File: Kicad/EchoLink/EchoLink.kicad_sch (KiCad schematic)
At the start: 37 parts, among them U1 STM32L433CCT6

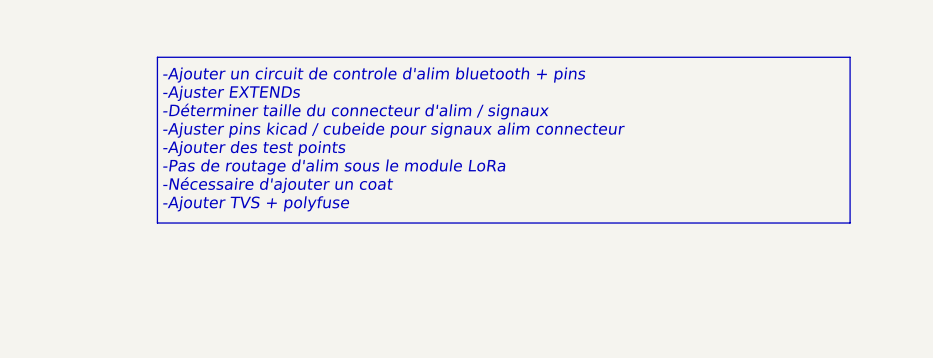
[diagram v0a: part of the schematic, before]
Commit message: wip: rename compoents
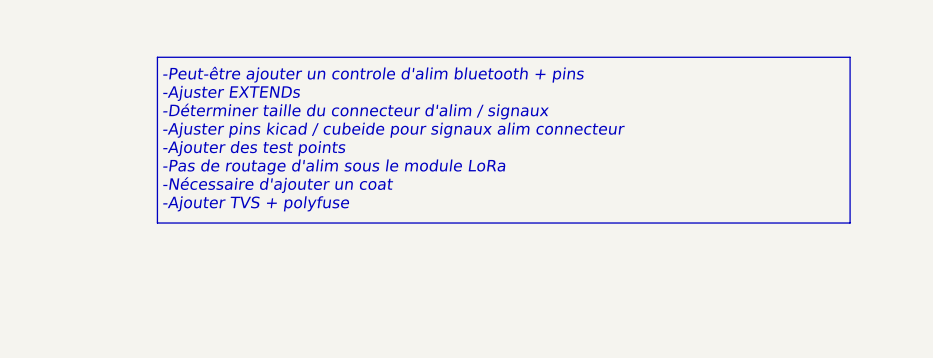
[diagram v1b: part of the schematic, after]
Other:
- note added: "-Peut-être ajouter un controle d'alim bluetooth + pins -Ajuster EXTENDs -Déterminer taille du connecteur d'alim / signaux -Ajuster pins kicad / cubeide pour signaux alim connecteur -Ajouter des test points -Pas de routage d'alim sous le module LoRa -Nécessaire d'ajouter un coat -Ajouter TVS + polyfuse"
- note removed: "-Ajouter un circuit de controle d'alim bluetooth + pins -Ajuster EXTENDs -Déterminer taille du connecteur d'alim / signaux -Ajuster pins kicad / cubeide pour signaux alim connecteur -Ajouter des test points -Pas de routage d'alim sous le module LoRa -Nécessaire d'ajouter un coat -Ajouter TVS + polyfuse"
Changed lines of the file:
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@@
 		)
 	)
-	(text "-Ajouter un circuit de controle d'alim bluetooth + pins\n-Ajuster EXTENDs\n-Déterminer taille du connecteur d'alim / signaux\n-Ajuster pins kicad / cubeide pour signaux alim connecteur\n-Ajouter des test points\n-Pas de routage d'alim sous le module LoRa\n-Nécessaire d'ajouter un coat\n-Ajouter TVS + polyfuse"
+	(text "-Peut-être ajouter un controle d'alim bluetooth + pins\n-Ajuster EXTENDs\n-Déterminer taille du connecteur d'alim / signaux\n-Ajuster pins kicad / cubeide pour signaux alim connecteur\n-Ajouter des test points\n-Pas de routage d'alim sous le module LoRa\n-Nécessaire d'ajouter un coat\n-Ajouter TVS + polyfuse"
 		(exclude_from_sim no)
 		(at 100.33 26.416 0)

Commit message: wip: connector and bms IOs
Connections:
- net EXTEND_IO1: no longer U1.30 (PA9)
- net EXTEND_IO2: no longer U1.31 (PA10)
- net EXTEND_IO3: no longer U1.32 (PA11)
- net EXTEND_IO4: no longer U1.33 (PA12)
- net POWER_IO1: no longer names the net of U1.5 (PH0-OSC_IN)
- net POWER_IO2: no longer names the net of U1.6 (PH1-OSC_OUT)
- net POWER_IO3: no longer names the net of U1.3 (PC14-OSC32_IN)
- net POWER_IO4: no longer names the net of U1.4 (PC15-OSC32_OUT)
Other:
- note added: "-Peut-être ajouter un controle d'alim bluetooth + pins -Ajuster EXTENDs -Connecteur entrant: 4x IOs relais (1x horn, 2x start engine, 1x start engine feedback) 1x UART/RS232/485/CAN -Pas de routage d'alim sous le module LoRa -Nécessaire d'ajouter un coat -Ajouter TVS + polyfuse -Possibilité de remplacer 3 entrées WKUP par 1 avec un OR 3-gates"
- note removed: "-Peut-être ajouter un controle d'alim bluetooth + pins -Ajuster EXTENDs -Déterminer taille du connecteur d'alim / signaux -Ajuster pins kicad / cubeide pour signaux alim connecteur -Ajouter des test points -Pas de routage d'alim sous le module LoRa -Nécessaire d'ajouter un coat -Ajouter TVS + polyfuse"

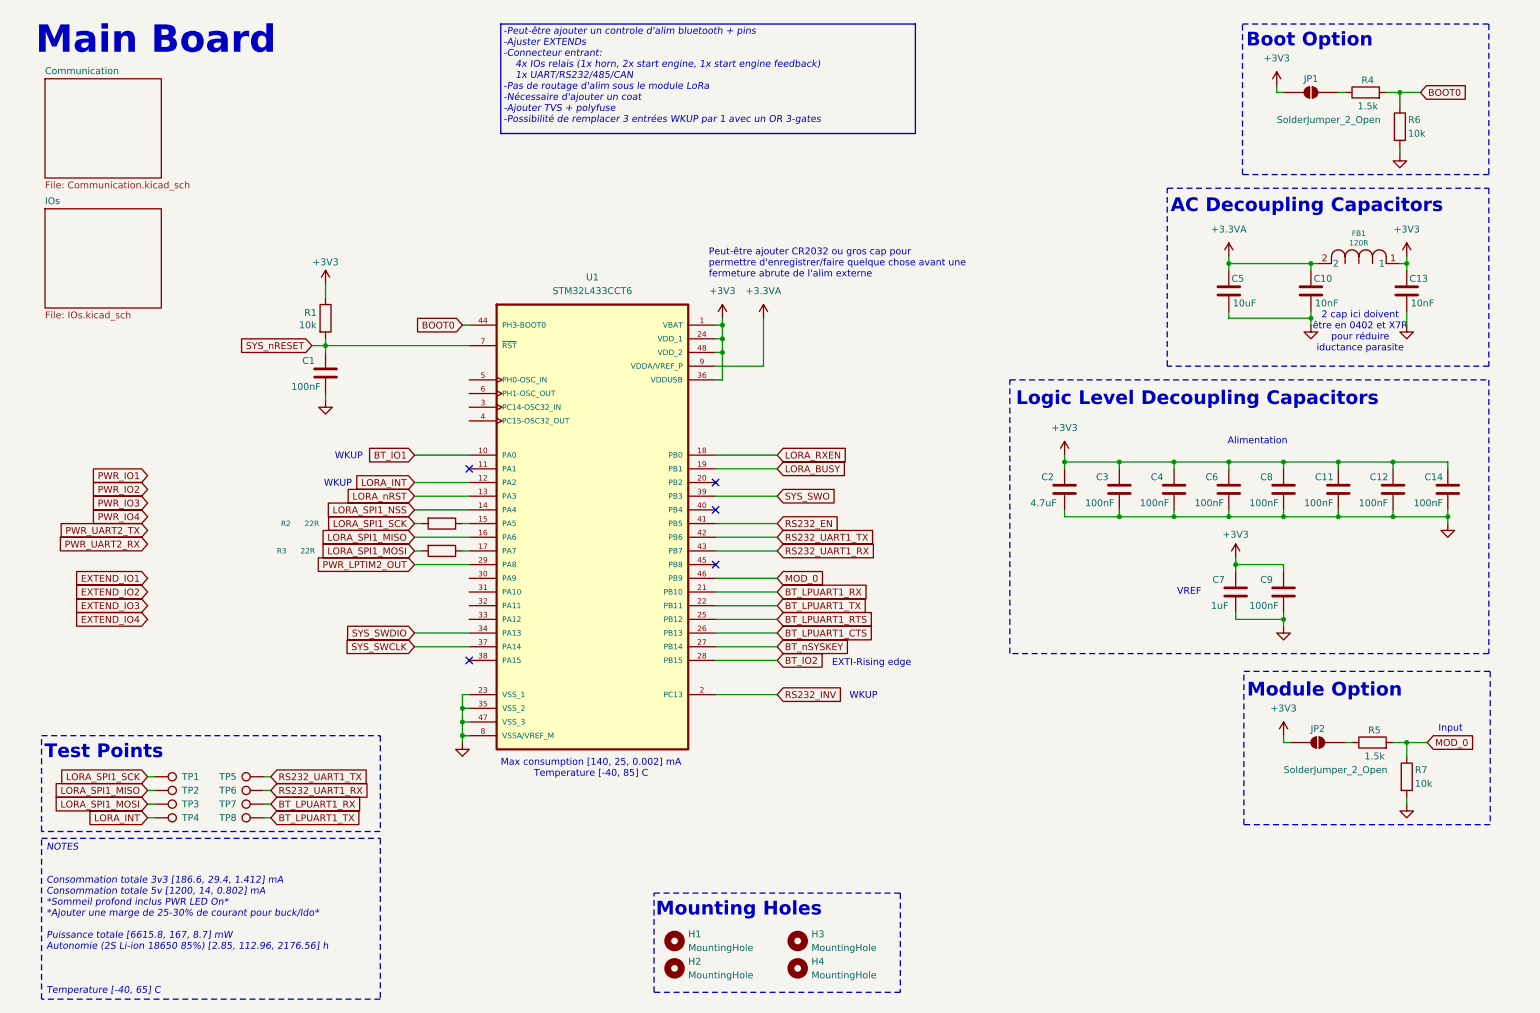
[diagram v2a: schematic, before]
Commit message: fix: rework all schematics to fit with new design and update stm32cubemx project
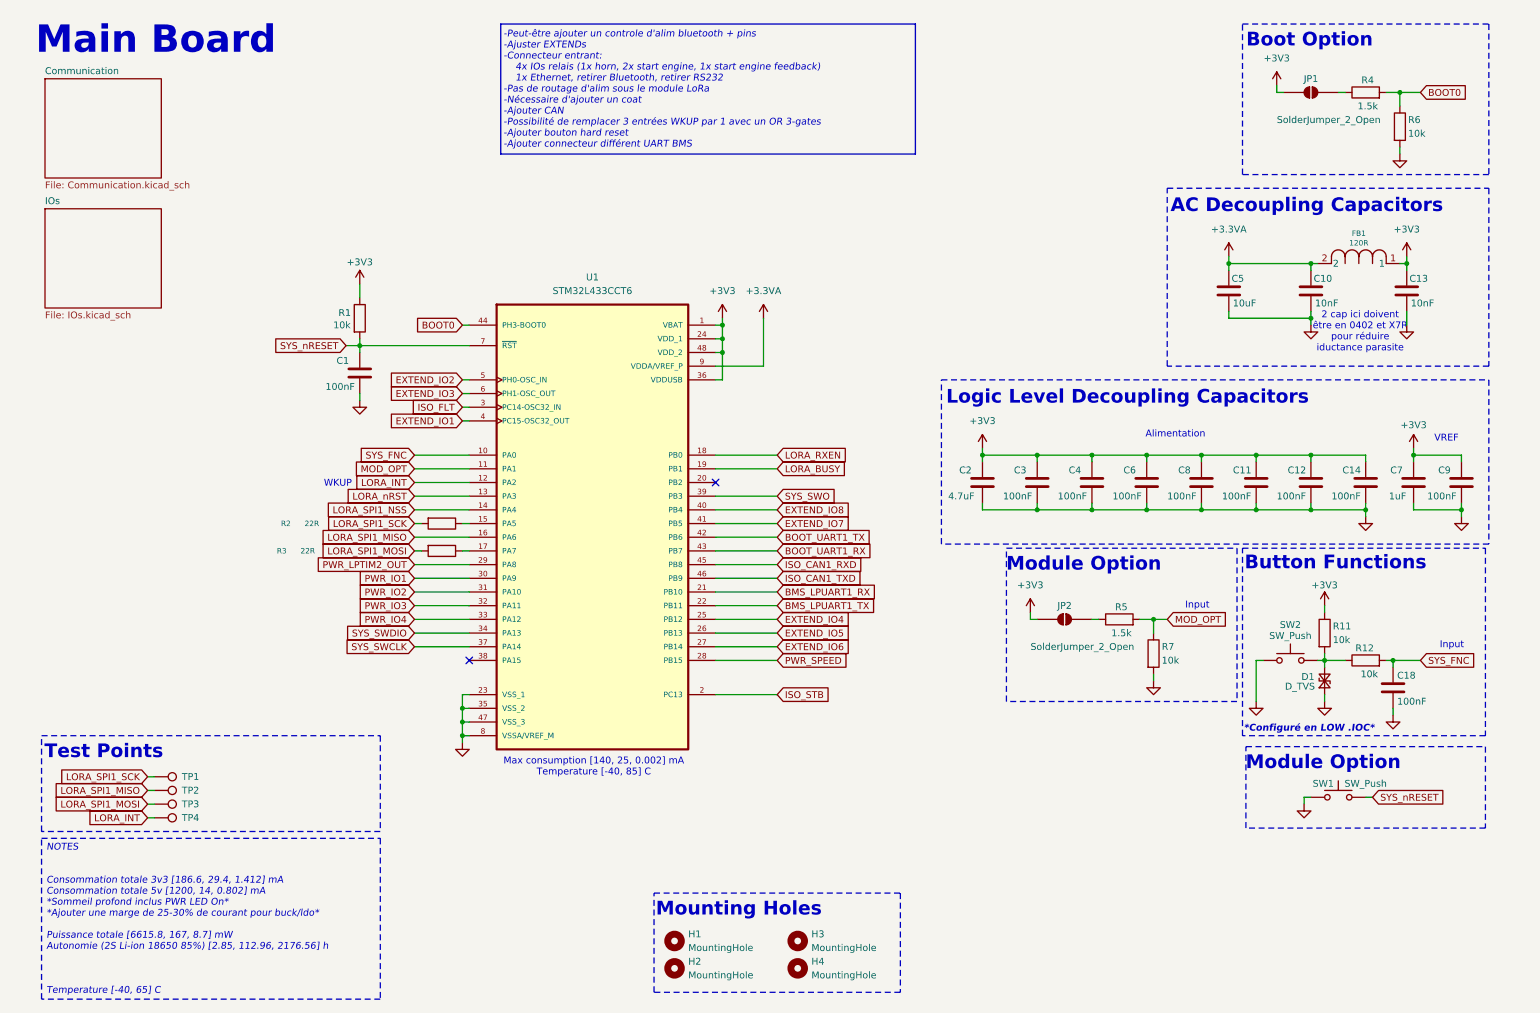
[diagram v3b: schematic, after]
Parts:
- removed TP5, TP6, TP7, TP8: TestPoint, TestPoint:TestPoint_Pad_D1.0mm, symbol Connector:TestPoint
- added C18: 100nF, Capacitor_SMD:C_0603_1608Metric, symbol Device:C
- added D1: D_TVS, symbol Device:D_TVS_Small
- added R11, R12: 10k, Resistor_SMD:R_0603_1608Metric, symbol Device:R
- added SW1, SW2: SW_Push, Package_SO:SOIC-8_3.9x4.9mm_P1.27mm, symbol Switch:SW_Push
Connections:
- net BT_LPUART1_RTS is gone; now on net EXTEND_IO4: U1.25 (PB12)
- net +3V3: now also R11.1
- net EXTEND_IO1: now also U1.4 (PC15-OSC32_OUT)
- net EXTEND_IO2: now also U1.5 (PH0-OSC_IN)
- net EXTEND_IO3: now also U1.6 (PH1-OSC_OUT)
- net GND: now also C18.2, D1.1 (A1), SW1.1, SW2.1
- net PWR_IO1: now also U1.30 (PA9)
- net PWR_IO2: now also U1.31 (PA10)
- net PWR_IO3: now also U1.32 (PA11)
- net PWR_IO4: now also U1.33 (PA12)
- net SYS_nRESET: now also SW1.2
- net MOD_OPT: now reaches U1.11 (PA1)
- net MOD_OPT: now also R5.2, R7.1
- net ISO_FLT: now reaches U1.3 (PC14-OSC32_IN)
- net EXTEND_IO8: now reaches U1.40 (PB4)
- net ISO_CAN1_RXD: now reaches U1.45 (PB8)
- net BT_IO1 renamed SYS_FNC
- net SYS_FNC: now also C18.1, R12.2
- net BT_IO2 renamed PWR_SPEED
- net BT_LPUART1_CTS renamed EXTEND_IO5
- net BT_LPUART1_RX renamed BMS_LPUART1_RX
- net BT_LPUART1_TX renamed BMS_LPUART1_TX
- net BT_nSYSKEY renamed EXTEND_IO6
- removed net MOD_0: R5.2, R7.1, U1.46 (PB9)
- net RS232_EN renamed EXTEND_IO7
- net RS232_INV renamed ISO_STB
- net RS232_UART1_RX renamed BOOT_UART1_RX
- net RS232_UART1_TX renamed BOOT_UART1_TX
- new net: D1.2 (A2), R11.2, R12.1, SW2.2
- new net ISO_CAN1_TXD: U1.46 (PB9)
- no-connect marks 5 -> 2
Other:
- note added: "*Configuré en LOW .IOC*"
- note added: "-Peut-être ajouter un controle d'alim bluetooth + pins -Ajuster EXTENDs -Connecteur entrant: 4x IOs relais (1x horn, 2x start engine, 1x start engine feedback) 1x Ethernet, retirer Bluetooth, retirer RS232 -Pas de routage d'alim sous le module LoRa -Nécessaire d'ajouter un coat -Ajouter CAN -Possibilité de remplacer 3 entrées WKUP par 1 avec un OR 3-gates -Ajouter bouton hard reset -Ajouter conne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"
- note added: "Button Functions"
- note removed: "-Peut-être ajouter un controle d'alim bluetooth + pins -Ajuster EXTENDs -Connecteur entrant: 4x IOs relais (1x horn, 2x start engine, 1x start engine feedback) 1x UART/RS232/485/CAN -Pas de routage d'alim sous le module LoRa -Nécessaire d'ajouter un coat -Ajouter TVS + polyfuse -Possibilité de remplacer 3 entrées WKUP par 1 avec un OR 3-gates"
- note removed: "EXTI-Rising edge"
- note removed: "Peut-être ajouter CR2032 ou gros cap pour permettre d'enregistrer/faire quelque chose avant une fermeture abrute de l'alim externe"
- moved on the sheet: C1, C11, C12, C14, C2, C3, C4, C6, C7, C8, C9, JP2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

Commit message: wip: add missing footprints
- connectors missing
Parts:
- added TP10, TP11, TP5, TP6, TP7, TP8, TP9: TestPoint, TestPoint:TestPoint_Pad_D1.0mm, symbol Connector:TestPoint
- D1, FB1: footprint (none) -> Resistor_SMD:R_0805_2012Metric
- SW1: renamed from SW2; footprint Package_SO:SOIC-8_3.9x4.9mm_P1.27mm -> EchoLink_Lib:SON4_PTS526 SM15 SMTR2 LFS_CNK
- SW2: renamed from SW1; footprint Package_SO:SOIC-8_3.9x4.9mm_P1.27mm -> EchoLink_Lib:SON4_PTS526 SM15 SMTR2 LFS_CNK
- U1: footprint STM32L433CCT6:QFP50P900X900X160-48N -> EchoLink_Lib:QFP50P900X900X160-48N
- renumbered C12 to C10, C14 to C11, C18 to C12, C7 to C14, C9 to C15, C6 to C5, C8 to C6, C5 to C7, C11 to C8, C10 to C9, JP2 to JP1, JP1 to JP2, R5 to R4, R7 to R5, R11 to R6, R4 to R7, R12 to R8, R6 to R9
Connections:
- net BMS_LPUART1_RX: now also TP9.1
- net BMS_LPUART1_TX: now also TP8.1
- net ISO_CAN1_RXD: now also TP5.1
- net ISO_CAN1_TXD: now also TP6.1
- net ISO_FLT renamed ISO_FNC
- net ISO_FNC: now also TP7.1
- new net EXTEND_UART1_RX: TP11.1
- new net EXTEND_UART1_TX: TP10.1
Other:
- note added: "-Pas de routage d'alim sous le module LoRa -Nécessaire d'ajouter un coat -Vérifier TVS"
- note removed: "-Peut-être ajouter un controle d'alim bluetooth + pins -Ajuster EXTENDs -Connecteur entrant: 4x IOs relais (1x horn, 2x start engine, 1x start engine feedback) 1x Ethernet, retirer Bluetooth, retirer RS232 -Pas de routage d'alim sous le module LoRa -Nécessaire d'ajouter un coat -Ajouter CAN -Possibilité de remplacer 3 entrées WKUP par 1 avec un OR 3-gates -Ajouter bouton hard reset -Ajouter conne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"
- note removed: "2 cap ici doivent être en 0402 et X7R pour réduire iductance parasite"
- moved on the sheet: TP1, TP2, TP3, TP4

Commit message: wip: ERC
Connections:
- net BOOT_UART1_RX is gone; now on net EXTEND_UART1_RX: U1.43 (PB7)
- net BOOT_UART1_TX is gone; now on net EXTEND_UART1_TX: U1.42 (PB6)
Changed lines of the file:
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@@
 		)
 	)
-	(global_label "BOOT_UART1_TX"
+	(global_label "EXTEND_UART1_TX"
 		(shape input)
 		(at 151.13 110.49 0)
@@
 		)
 	)
-	(global_label "BOOT_UART1_RX"
+	(global_label "EXTEND_UART1_RX"
 		(shape input)
 		(at 151.13 113.03 0)
@@
 		)
 		(property "Intersheetrefs" "${INTERSHEET_REFS}"
-			(at 169.2947 113.03 0)
-			(hide yes)
-			(show_name no)
+			(at 171.4717 113.03 0)
+			(hide yes)
+			(show_name no)

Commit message: wip: add hse crystal and update stm32 project (clock 80MHz and 500kbps CAN)
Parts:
- added C10, C14: 22pF, Capacitor_SMD:C_0603_1608Metric, symbol Device:C
- added R10: 10R, Resistor_SMD:R_0603_1608Metric, symbol Device:R
- added Y1: WE-XTAL_HC49, EchoLink_Lib:WE-XTAL_HC49, symbol EchoLink_lib:WE-XTAL_HC49
- renumbered C12 to C1, C9 to C11, C10 to C12, C11 to C13, C13 to C15, C14 to C16, C15 to C17, C1 to C2, C2 to C3, C3 to C4, C4 to C5, C5 to C6, C6 to C7, C7 to C8, C8 to C9, R6 to R1, R4 to R2, R8 to R3, R5 to R4, R1 to R5, R2 to R6, R3 to R7, R7 to R8
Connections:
- net GND: now also C10.1, C14.1
- net EXTEND_IO1: no longer names the net of U1.4 (PC15-OSC32_OUT)
- net EXTEND_IO2 renamed OSC_IN
- net OSC_IN: now also C10.2, Y1.1
- net EXTEND_IO3 renamed OSC_OUT
- net OSC_OUT: now also R10.2
- new net: C14.2, R10.1, Y1.2
- no-connect marks 2 -> 3
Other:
- note added: "8MHz->CAN Controller stabilization"
- note added: "C_load = (C1 x C2)/(C1 + C2) + C_parasite C1, C2 >= 22pF si C_load = 18pF et C_parasite = 3pF ESR max <= 40ohms"
- note added: "External Crystal"
- moved on the sheet: C1, C2, D1, JP1, R1, R2, R3, R4, R5, R6, R7, SW1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
